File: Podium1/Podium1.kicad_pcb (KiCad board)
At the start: 2 copper layers, 56.6 x 53.5 mm, 7 parts

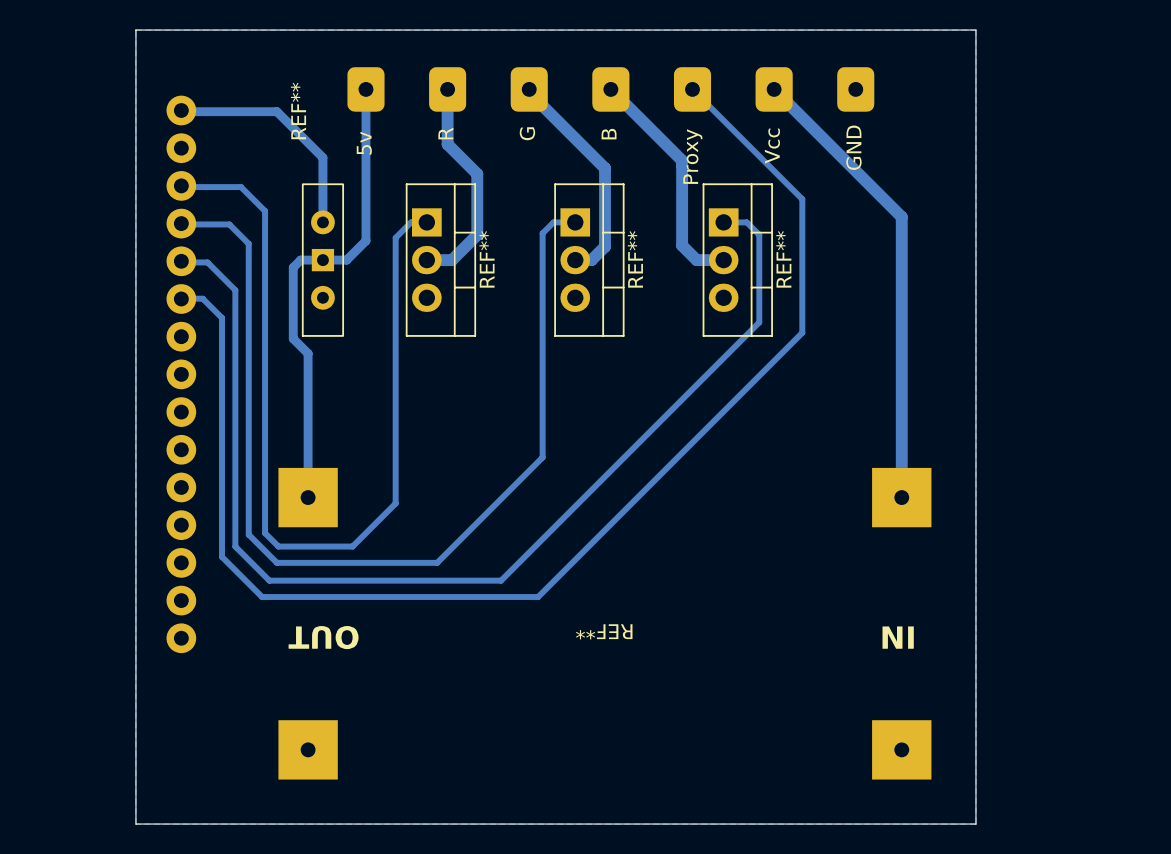
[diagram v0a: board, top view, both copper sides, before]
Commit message: PCB without ground pour
Modified PCB design to exclude ground pour and have 0.6mm clearance.
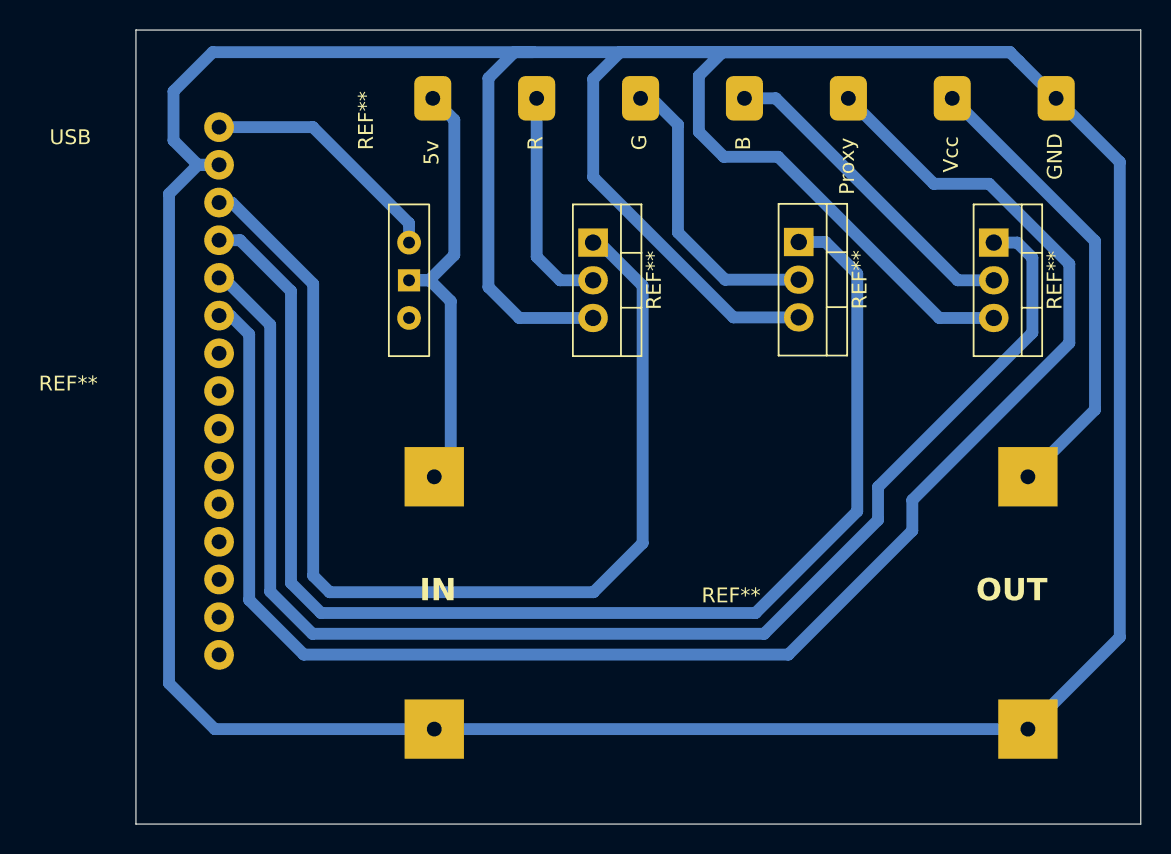
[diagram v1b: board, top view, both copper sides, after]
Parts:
- moved REF** 18.3 mm to (115.2, 96.8)
- moved REF** 15.1 mm to (102.1, 96.8)
- moved REF** 11.3 mm to (88.2, 96.8)
- moved REF** 8.61 mm to (97.5, 121.1), turned to 0 degrees
- moved REF** 5.96 mm to (75.8, 99.4)
- moved REF** 4.54 mm to (75.9, 88.6)
- moved REF** 2.78 mm to (52.8, 106.8)
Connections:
- REF** pad 1: (no net) -> 5vs
- REF** pad 3: (no net) -> Rp
- REF** pad 4: (no net) -> Gp
- REF** pad 5: (no net) -> Bp
- REF** pad 6: (no net) -> Proxy
- REF** pad 1: GND -> 5v
- REF** pad 2: (no net) -> GND
- REF** pad 3: (no net) -> GND
- REF** pad 4: GND -> Vcc
- REF** pad 1: (no net) -> Bp
- REF** pad 2: (no net) -> Bg
- REF** pad 1: (no net) -> Rp
- REF** pad 2: (no net) -> Rg (x2)
- REF** pad 1: (no net) -> Gp
- REF** pad 2: (no net) -> Gg
- REF** pad 1: (no net) -> 5v (x2)
- REF** pad 3: (no net) -> Gg
- REF** pad 4: (no net) -> Bg
- REF** pad 5: (no net) -> Proxy
- REF** pad 6: (no net) -> Vcc
- REF** pad 3: (no net) -> 5vs
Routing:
- net (no net): track 408.5 -> 0.00 mm
- net GND: track 0.00 -> 341.5 mm
- net Proxy: track 0.00 -> 112.0 mm
- net Bp: track 0.00 -> 93.0 mm
- net Gp: track 0.00 -> 88.6 mm
- net Rp: track 0.00 -> 74.2 mm
- net Vcc: track 0.00 -> 31.4 mm
- net 5v: track 0.00 -> 30.6 mm
- net Bg: track 0.00 -> 21.9 mm
- net Gg: track 0.00 -> 20.0 mm
- net 5vs: track 0.00 -> 16.8 mm
- net Rg: track 0.00 -> 15.1 mm
- removed copper zone on B.Cu, net GND
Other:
- board size 56.6 x 53.5 mm -> 67.7 x 53.5 mm
